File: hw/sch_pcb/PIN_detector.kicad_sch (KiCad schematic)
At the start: 37 parts, among them Q1 2SK2394-6, U2 AD8691, U3 ISL21080DIH309, U3 SHT31-DIS, U8 OPA314

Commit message: Update silkscreen and title blocks.
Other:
- title: AIRDOS04A base board -> USTSIPIN03A

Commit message: Fix USTID
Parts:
- C17, C59: UST_ID 5c70984812875079b91f8bf2 -> 5c70984712875079b91f8b4c
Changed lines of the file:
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@@
       (effects (font (size 1.27 1.27)) hide)
     )
-    (property "UST_ID" "5c70984812875079b91f8bf2" (at 40.64 154.94 0)
+    (property "UST_ID" "5c70984712875079b91f8b4c" (at 40.64 154.94 0)
       (effects (font (size 1.27 1.27)) hide)
     )
@@
       (effects (font (size 1.27 1.27)) hide)
     )
-    (property "UST_ID" "5c70984812875079b91f8bf2" (at -215.9 62.23 0)
-      (effects (font (size 1.27 1.27)) hide)
-    )
+    (property "UST_ID" "5c70984712875079b91f8b4c" (at -215.9 62.23 0)
+      (effects (font (size 1.27 1.27)) hide)
+    )

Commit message: FIX USTIDs.
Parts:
- R9: UST_ID (none) -> 5c70984612875079b91f899f
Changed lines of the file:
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@@
       (effects (font (size 1.27 1.27)) hide)
     )
-    (property "UST_ID" "" (at 195.58 132.08 0)
+    (property "UST_ID" "5c70984612875079b91f899f" (at 195.58 132.08 0)
       (effects (font (size 1.27 1.27)) hide)
     )

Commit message: Add notes to power consumption.
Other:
- note added: "+300 uA"
- note added: "1.2 mA"
- note added: "1.5uA"
- note added: "2uA"
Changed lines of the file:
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@@
+    (effects (font (size 1.524 1.524)) (justify left bottom))
+  )
+  (text "2uA" (at 44.45 29.21 0)
     (effects (font (size 1.524 1.524)) (justify left bottom))
   )
@@
   (text "REF 0.9 V is the lowest value of\nreasonably available voltage reference."
     (at 62.23 168.91 0)
+    (effects (font (size 1.524 1.524)) (justify left bottom))
+  )
+  (text "1.5uA" (at 54.61 135.89 0)
+    (effects (font (size 1.524 1.524)) (justify left bottom))
+  )
+  (text "1.2 mA" (at 198.12 80.01 0)
+    (effects (font (size 1.524 1.524)) (justify left bottom))
+  )
+  (text "+300 uA" (at 156.21 116.84 0)
     (effects (font (size 1.524 1.524)) (justify left bottom))
   )
@@
       (effects (font (size 1.27 1.27) italic) hide)
     )
-    (property "Datasheet" "http://www.intersil.com/content/dam/Intersil/documents/fn75/fn7599.pdf" (at 54.61 157.48 0)
+    (property "Datasheet" "https://www.renesas.com/us/en/document/dst/isl21080-datasheet" (at 54.61 157.48 0)
       (effects (font (size 1.27 1.27) italic) hide)
     )

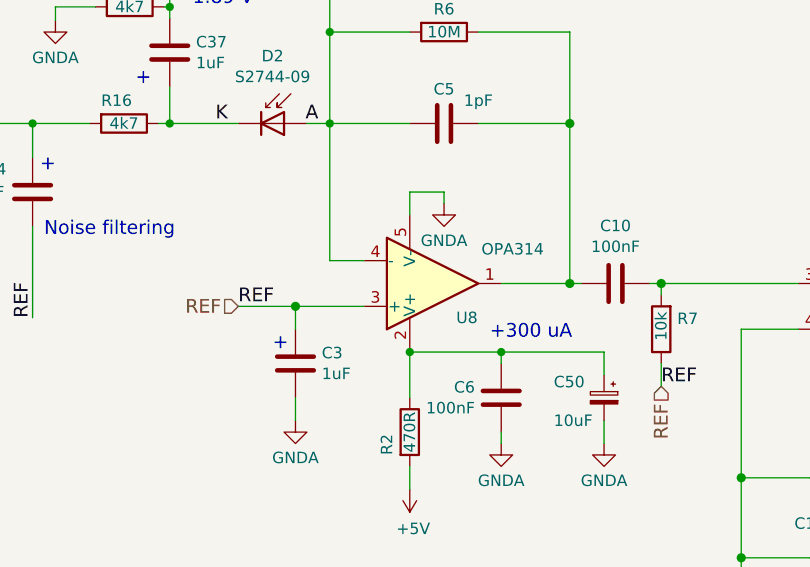
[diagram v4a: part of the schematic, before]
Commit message: Swap power pins of input OpAMP. Reslove #6
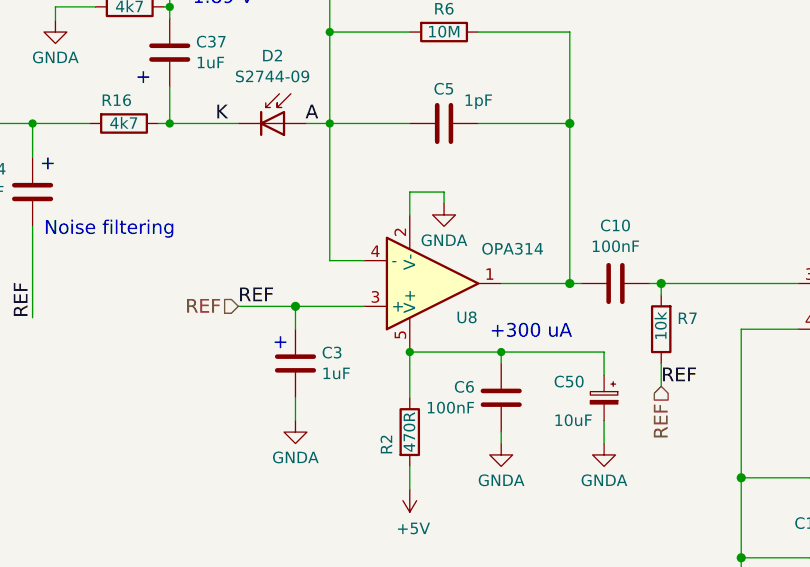
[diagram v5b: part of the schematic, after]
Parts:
- U8: symbol Amplifier_Operational:MCP6001R -> MLAB_IO:OPA314
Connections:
- net GNDA: now also U8.2 (V-); no longer U8.5 (V-)
- net at C50.1, C6.1, R2.1: now also U8.5 (V+); no longer U8.2 (V+)
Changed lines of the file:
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@@
     )
   )
-  (symbol (lib_id "Amplifier_Operational:MCP6001R") (at 149.86 110.49 0) (mirror x) (unit 1)
+  (symbol (lib_id "MLAB_IO:OPA314") (at 149.86 110.49 0) (mirror x) (unit 1)
     (in_bom yes) (on_board yes) (dnp no)
     (property "Reference" "U8" (at 153.67 114.3 0)
@@
       (effects (font (size 1.27 1.27)))
     )
-    (property "Footprint" "Package_TO_SOT_SMD:SOT-23-5" (at 149.86 110.49 0)
+    (property "Footprint" "Package_TO_SOT_SMD:SOT-23-5" (at 148.59 113.03 0)
       (effects (font (size 1.27 1.27)) hide)
     )
-    (property "Datasheet" "https://www.ti.com/lit/ds/symlink/opa314.pdf" (at 149.86 115.57 0)
+    (property "Datasheet" "https://www.ti.com/lit/ds/symlink/opa314.pdf" (at 151.13 115.57 0)
       (effects (font (size 1.27 1.27)) hide)
     )

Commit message: Removed hand-soldering footprints for OpAmps. Rosolve #1
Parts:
- U2: footprint Package_TO_SOT_SMD:TSOT-23-5_HandSoldering -> Package_TO_SOT_SMD:TSOT-23-5
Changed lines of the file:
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@@
       (effects (font (size 1.27 1.27)) (justify left))
     )
-    (property "Footprint" "Package_TO_SOT_SMD:TSOT-23-5_HandSoldering" (at 198.12 113.03 0)
+    (property "Footprint" "Package_TO_SOT_SMD:TSOT-23-5" (at 198.12 113.03 0)
       (effects (font (size 1.27 1.27)) hide)
     )

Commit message: Update Kicad project version.
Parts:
- renumbered U2 to U9
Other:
- company: Jakub Kákona <info@ust.cz> -> kaklik <info@ust.cz>
- title: USTSIPIN03A -> USTSIPIN03B
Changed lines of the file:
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@@
   (paper "A4")
   (title_block
-    (title "USTSIPIN03A")
+    (title "USTSIPIN03B")
     (date "2023-10-23")
-    (company "Jakub Kákona <info@ust.cz>")
+    (company "kaklik <info@ust.cz>")
     (comment 2 "Semiconductor\\nionizing radiation detector")
   )
@@
       )
       (project "USTSIPIN03"
-        (path "/e63e39d7-6ac0-4ffd-8aa3-1841a4541b55"
-          (reference "C22") (unit 1)
-        )
-        (path "/e63e39d7-6ac0-4ffd-8aa3-1841a4541b55/5c006114-f78d-4936-a365-c4e7307459e1"
-          (reference "C25") (unit 1)
-        )
         (path "/e63e39d7-6ac0-4ffd-8aa3-1841a4541b55/e191f86f-5b54-4b8b-aca6-37b81226f3b6"
           (reference "C36") (unit 1)
@@
         (path "/e63e39d7-6ac0-4ffd-8aa3-1841a4541b55/e191f86f-5b54-4b8b-aca6-37b81226f3b6"
           (reference "#PWR033") (unit 1)
-        )
-        (path "/e63e39d7-6ac0-4ffd-8aa3-1841a4541b55/5c006114-f78d-4936-a365-c4e7307459e1"
-          (reference "#PWR067") (unit 1)
         )
       )
@@
   (symbol (lib_id "MLAB_IO:AD8691") (at 198.12 113.03 0) (unit 1)
     (in_bom yes) (on_board yes) (dnp no)
-    (property "Reference" "U2" (at 199.39 109.22 0)
+    (property "Reference" "U9" (at 199.39 109.22 0)
       (effects (font (size 1.27 1.27)) (justify left))
     )
@@
     (instances
       (project "USTSIPIN03"
-        (path "/e63e39d7-6ac0-4ffd-8aa3-1841a4541b55"
-          (reference "U2") (unit 1)
-        )
-        (path "/e63e39d7-6ac0-4ffd-8aa3-1841a4541b55/5c006114-f78d-4936-a365-c4e7307459e1"
-          (reference "U1") (unit 1)
-        )
         (path "/e63e39d7-6ac0-4ffd-8aa3-1841a4541b55/e191f86f-5b54-4b8b-aca6-37b81226f3b6"
           (reference "U9") (unit 1)
@@
         (path "/e63e39d7-6ac0-4ffd-8aa3-1841a4541b55/e191f86f-5b54-4b8b-aca6-37b81226f3b6"
           (reference "#PWR054") (unit 1)
-        )
-        (path "/e63e39d7-6ac0-4ffd-8aa3-1841a4541b55/5c006114-f78d-4936-a365-c4e7307459e1"
-          (reference "#PWR067") (unit 1)
         )
       )
@@
       )
       (project "USTSIPIN03"
-        (path "/e63e39d7-6ac0-4ffd-8aa3-1841a4541b55"
-          (reference "U4") (unit 1)
-        )
-        (path "/e63e39d7-6ac0-4ffd-8aa3-1841a4541b55/5c006114-f78d-4936-a365-c4e7307459e1"
-          (reference "U6") (unit 1)
-        )
         (path "/e63e39d7-6ac0-4ffd-8aa3-1841a4541b55/e191f86f-5b54-4b8b-aca6-37b81226f3b6"
           (reference "U10") (unit 1)
@@
         (path "/e63e39d7-6ac0-4ffd-8aa3-1841a4541b55/e191f86f-5b54-4b8b-aca6-37b81226f3b6"
           (reference "#PWR040") (unit 1)
-        )
-        (path "/e63e39d7-6ac0-4ffd-8aa3-1841a4541b55/5c006114-f78d-4936-a365-c4e7307459e1"
-          (reference "#PWR067") (unit 1)
         )
       )
@@
       )
       (project "USTSIPIN03"
-        (path "/e63e39d7-6ac0-4ffd-8aa3-1841a4541b55"
-          (reference "#PWR040") (unit 1)
-        )
-        (path "/e63e39d7-6ac0-4ffd-8aa3-1841a4541b55/5c006114-f78d-4936-a365-c4e7307459e1"
-          (reference "#PWR042") (unit 1)
-        )
         (path "/e63e39d7-6ac0-4ffd-8aa3-1841a4541b55/e191f86f-5b54-4b8b-aca6-37b81226f3b6"
           (reference "#PWR055") (unit 1)
@@
         (path "/e63e39d7-6ac0-4ffd-8aa3-1841a4541b55/e191f86f-5b54-4b8b-aca6-37b81226f3b6"
           (reference "#PWR053") (unit 1)
-        )
-        (path "/e63e39d7-6ac0-4ffd-8aa3-1841a4541b55/5c006114-f78d-4936-a365-c4e7307459e1"
-          (reference "#PWR067") (unit 1)
         )
       )
@@
   (symbol (lib_id "power:GNDA") (at 52.07 167.64 0) (unit 1)
     (in_bom yes) (on_board yes) (dnp no)
-    (property "Reference" "#PWR014" (at 52.07 173.99 0)
+    (property "Reference" "#PWR056" (at 52.07 173.99 0)
       (effects (font (size 1.27 1.27)) hide)
     )
@@
     (instances
       (project "USTSIPIN03"
-        (path "/e63e39d7-6ac0-4ffd-8aa3-1841a4541b55"
-          (reference "#PWR014") (unit 1)
-        )
-        (path "/e63e39d7-6ac0-4ffd-8aa3-1841a4541b55/5c006114-f78d-4936-a365-c4e7307459e1"
-          (reference "#PWR043") (unit 1)
-        )
         (path "/e63e39d7-6ac0-4ffd-8aa3-1841a4541b55/e191f86f-5b54-4b8b-aca6-37b81226f3b6"
           (reference "#PWR056") (unit 1)
